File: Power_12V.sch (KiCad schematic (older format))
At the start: 5 parts

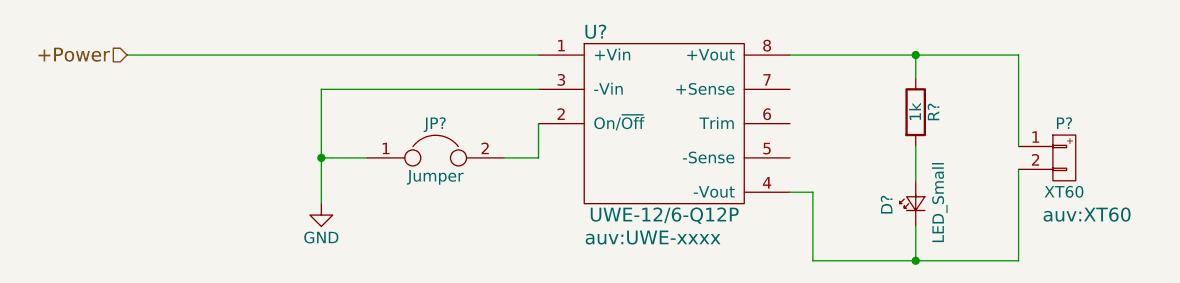
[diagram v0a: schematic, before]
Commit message: Correct all foot-print assignments
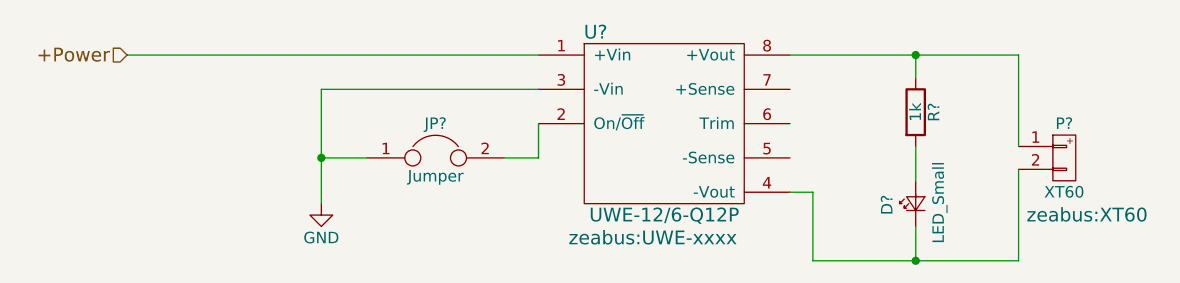
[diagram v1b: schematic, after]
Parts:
- P?: footprint auv:XT60 -> zeabus:XT60
- U?: footprint auv:UWE-xxxx -> zeabus:UWE-xxxx
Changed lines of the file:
@@
 $Descr A4 11693 8268
 encoding utf-8
-Sheet 5 12
+Sheet 5 13
 Title ""
 Date ""
@@
 F 0 "U?" H 5300 3800 60  0000 C CNN
 F 1 "UWE-12/6-Q12P" H 5600 3000 60  0000 C CNN
-F 2 "auv:UWE-xxxx" H 5550 2900 60  0000 C CNN
+F 2 "zeabus:UWE-xxxx" H 5550 2900 60  0000 C CNN
 F 3 "" H 5650 3100 60  0000 C CNN
 	1    5600 3400
@@
 F 0 "P?" H 7350 3700 50  0000 C CNN
 F 1 "XT60" H 7350 3400 50  0000 C CNN
-F 2 "auv:XT60" H 7450 3300 60  0000 C CNN
+F 2 "zeabus:XT60" H 7450 3300 60  0000 C CNN
 F 3 "" H 7350 3550 60  0000 C CNN
 	1    7350 3550

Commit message: Annotate all components
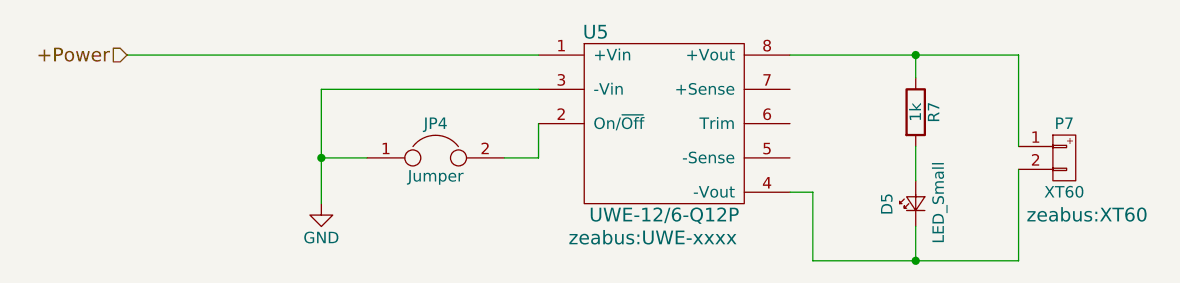
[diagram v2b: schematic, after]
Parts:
- gave numbers to parts that had none: 5
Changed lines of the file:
@@
 LIBS:zeabus
 LIBS:ftdi
-LIBS:Power_Distributor-cache
 EELAYER 25 0
 EELAYER END
@@
 $EndDescr
 $Comp
-L UWE-12/6-Q12P U?
+L UWE-12/6-Q12P U5
 U 1 1 58DFE00C
 P 5600 3400
-F 0 "U?" H 5300 3800 60  0000 C CNN
+F 0 "U5" H 5300 3800 60  0000 C CNN
 F 1 "UWE-12/6-Q12P" H 5600 3000 60  0000 C CNN
 F 2 "zeabus:UWE-xxxx" H 5550 2900 60  0000 C CNN
@@
 $EndComp
 $Comp
-L GND #PWR?
+L GND #PWR019
 U 1 1 58DFE329
 P 4100 3750
-F 0 "#PWR?" H 4100 3500 50  0001 C CNN
+F 0 "#PWR019" H 4100 3500 50  0001 C CNN
 F 1 "GND" H 4100 3600 50  0000 C CNN
 F 2 "" H 4100 3750 50  0001 C CNN
@@
 $EndComp
 $Comp
-L Jumper JP?
+L Jumper JP4
 U 1 1 58DFE33F
 P 4600 3550
-F 0 "JP?" H 4600 3700 50  0000 C CNN
+F 0 "JP4" H 4600 3700 50  0000 C CNN
 F 1 "Jumper" H 4600 3470 50  0000 C CNN
 F 2 "Pin_Headers:Pin_Header_Straight_1x02_Pitch2.00mm" H 4600 3550 50  0001 C CNN
@@
 Connection ~ 4100 3550
 $Comp
-L LED_Small D?
+L LED_Small D5
 U 1 1 58DFE475
 P 6700 3750
-F 0 "D?" H 6650 3875 50  0000 L CNN
+F 0 "D5" H 6650 3875 50  0000 L CNN
 F 1 "LED_Small" H 6525 3650 50  0000 L CNN
 F 2 "LEDs:LED_0603" V 6700 3750 50  0001 C CNN
@@
 $EndComp
 $Comp
-L R R?
+L R R7
 U 1 1 58DFE4C6
 P 6700 3350
-F 0 "R?" V 6780 3350 50  0000 C CNN
+F 0 "R7" V 6780 3350 50  0000 C CNN
 F 1 "1k" V 6700 3350 50  0000 C CNN
 F 2 "Resistors_SMD:R_0603" V 6630 3350 50  0001 C CNN
@@
 $EndComp
 $Comp
-L XT60 P?
+L XT60 P7
 U 1 1 58DFE4FF
 P 7350 3550
-F 0 "P?" H 7350 3700 50  0000 C CNN
+F 0 "P7" H 7350 3700 50  0000 C CNN
 F 1 "XT60" H 7350 3400 50  0000 C CNN
 F 2 "zeabus:XT60" H 7450 3300 60  0000 C CNN
